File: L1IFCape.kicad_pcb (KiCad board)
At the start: 2 copper layers, 86.4 x 54.6 mm, 72 parts, among them J1 RF_Shield_One_Piece, J2 SMA, J3 MMCX, P8 BeagleBone_Black_Header, P9 BeagleBone_Black_Header, U1 24CS256, U2 MAX2769BETI+T, U3 MAX31343ETAY+T, U4 TPS717285DCK, U5 TPS717285DCK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

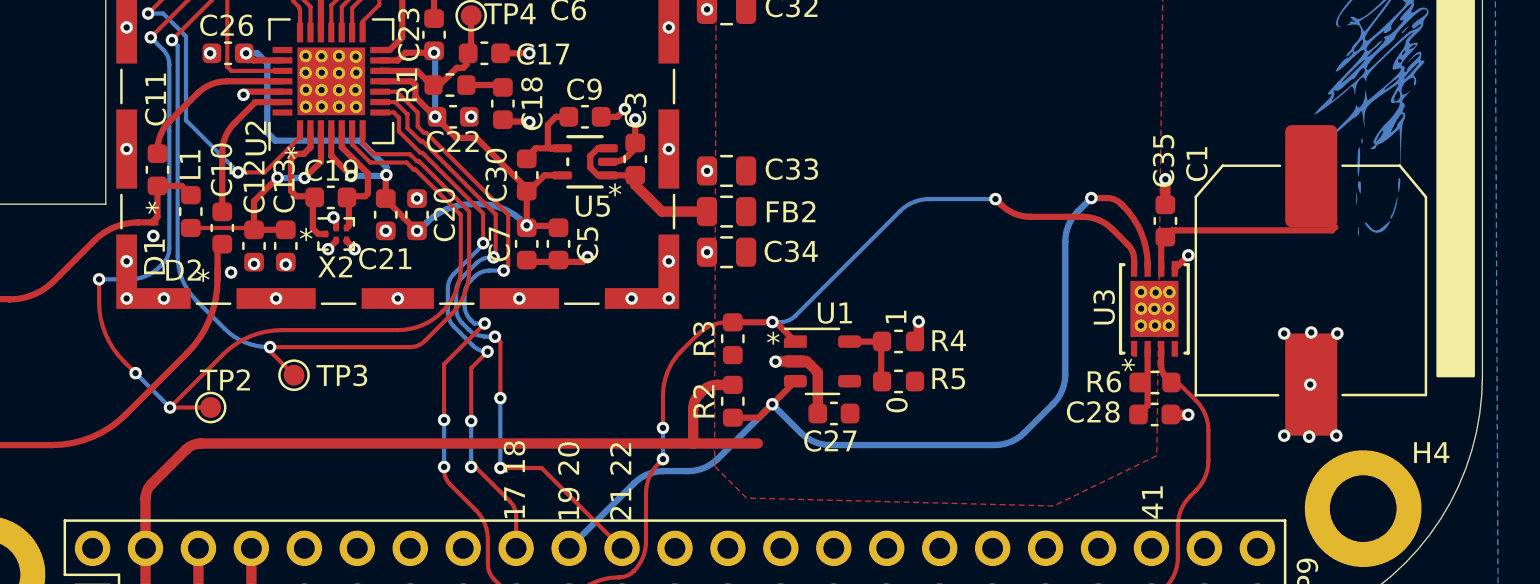
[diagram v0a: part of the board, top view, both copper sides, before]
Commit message: Added CERN License
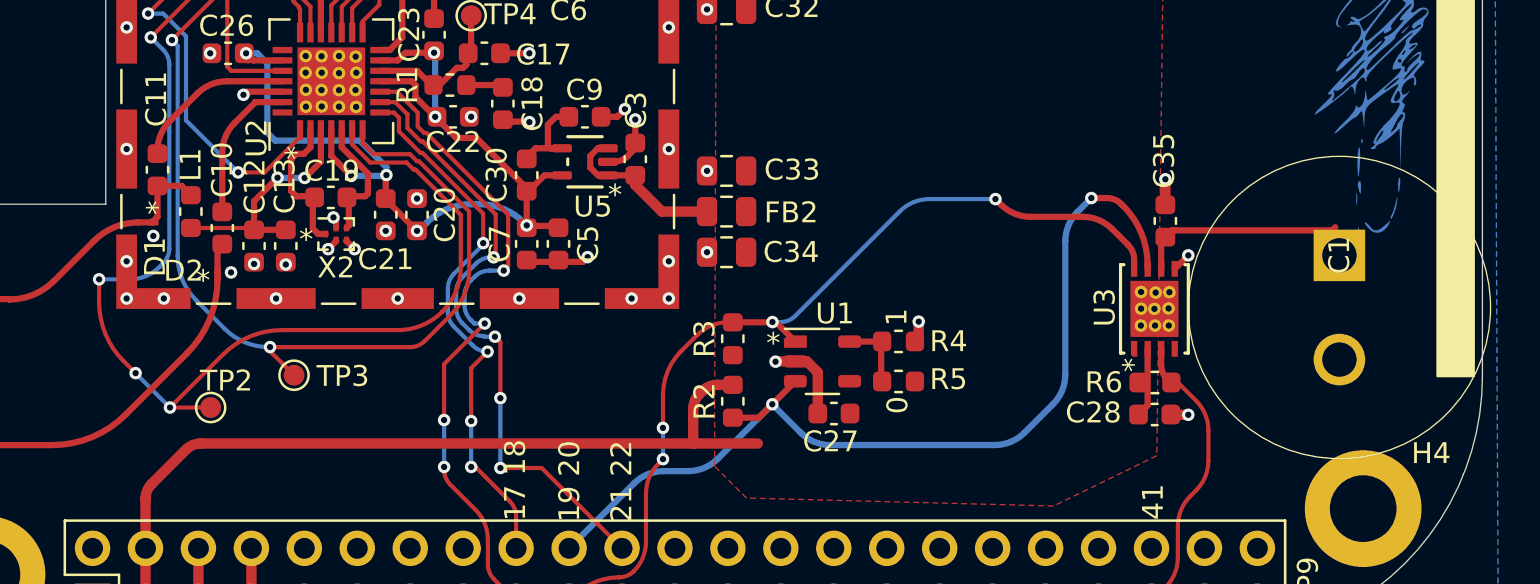
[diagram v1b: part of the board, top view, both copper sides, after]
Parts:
- C1: value 0.1 F -> 1F; footprint L1IF:C_EDLC_FCR_10.8x10.8 -> L1IF:CAPPRD500W145D1350H830
- moved C1 1.81 mm to (179.5, 81.5)
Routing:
- net GND: vias 69 -> 62

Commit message: Moved some parts around
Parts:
- moved TP2 34.4 mm to (125.8, 54.4)
- moved TP3 32.9 mm to (128.4, 54.4)
- moved C1 5.71 mm to (174.2, 83.8), turned to 0 degrees
- moved R6 3.48 mm to (167.9, 89.7)
- moved C35 3.07 mm to (168.1, 80.2)
- moved U3 3.07 mm to (167.6, 84.4)
- moved C28 2.93 mm to (167.9, 88.2)
- moved TP1 0.32 mm to (123.2, 54.4)
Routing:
- net /I2C0.SDA: track 46.5 -> 41.9 mm
- net /I2C0.SCL: track 42.7 -> 39.7 mm
- net /LD: track 77.1 -> 75.1 mm
- net /~{RTC_INTR}: track 14.8 -> 13.2 mm
- net /~{SHDN}: track 67.6 -> 66.0 mm
- net +3V3: track 43.1 -> 41.6 mm
- net Net-(U3-VBAT): track 9.95 -> 8.67 mm
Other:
- board text added: "*"

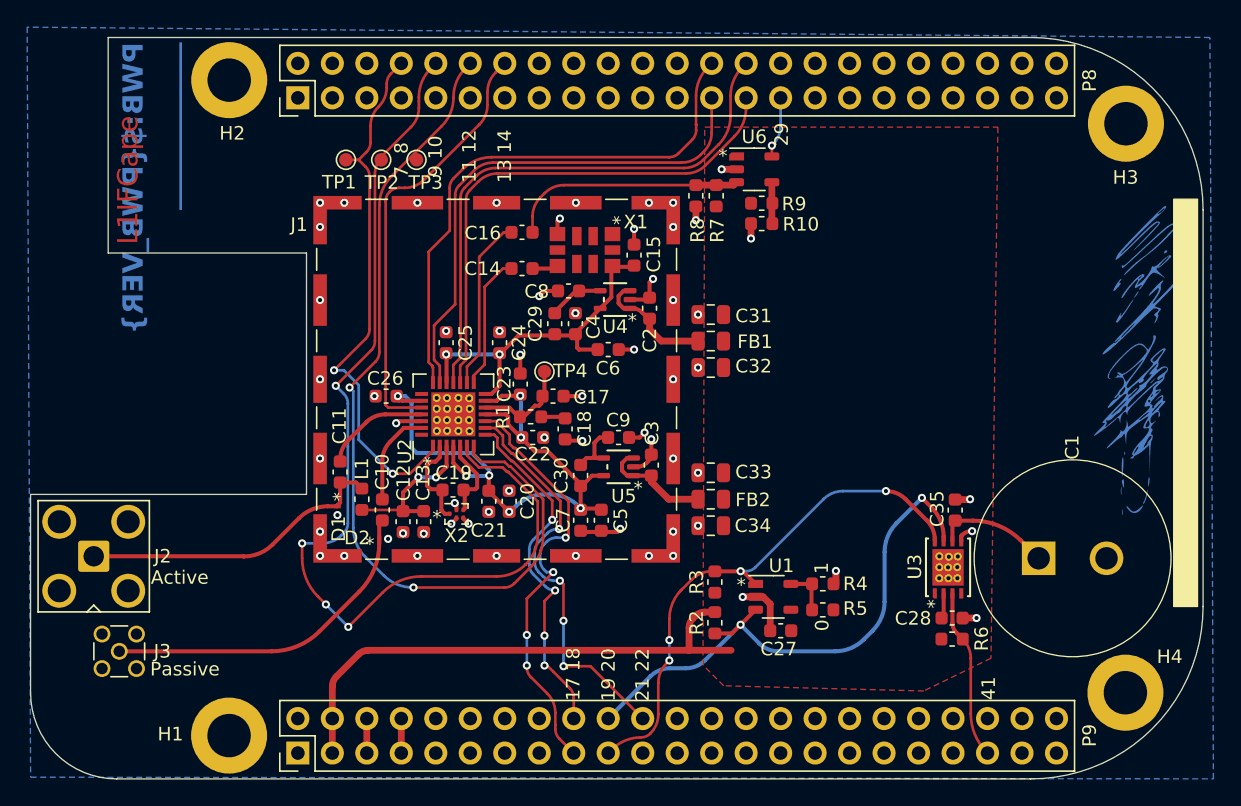
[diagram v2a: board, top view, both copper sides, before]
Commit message: Added Padlock graphic and 1F Supercap
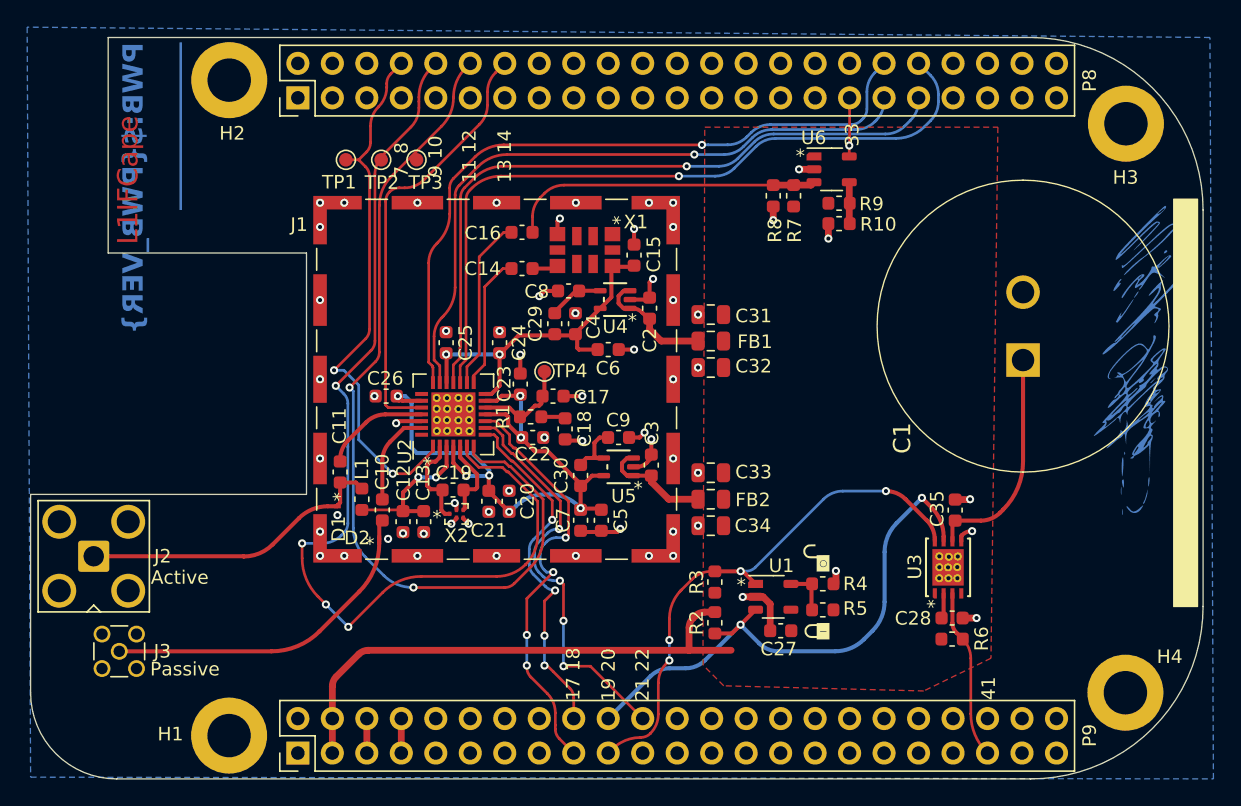
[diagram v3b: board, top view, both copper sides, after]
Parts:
- added G***: LOGO, L1IF:Padlock-On, F.Cu at (157.9, 88.7)
- added G***: LOGO, L1IF:Padlock-Off, F.Cu at (157.9, 83.7)
- C1: footprint L1IF:CAPPRD500W145D1350H830 -> L1IF:KR5R5C105R
- moved C1 14.6 mm to (173.1, 69.2), turned to 90 degrees
- moved R10 5.70 mm to (159.6, 59.1)
- moved R9 5.70 mm to (159.6, 57.6)
- moved R7 5.70 mm to (156.2, 57.0)
- moved R8 5.70 mm to (154.7, 57.0)
- moved U6 5.70 mm to (159.0, 55.1)
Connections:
- P8 pad 25: /SI0H -> unconnected-(P8-Pin_25-Pad25)
- P8 pad 26: /SI1H -> unconnected-(P8-Pin_26-Pad26)
- P8 pad 27: /SQ1H -> unconnected-(P8-Pin_27-Pad27)
- P8 pad 28: /SQ0H -> unconnected-(P8-Pin_28-Pad28)
- P8 pad 29: /BBClk -> unconnected-(P8-Pin_29-Pad29)
- P8 pad 33: /CLKIN_S_7 -> /BBClk
- P8 pad 35: /GPIO52PB1/LPRB_A -> /SI0H
- P8 pad 36: /GPIO37NB1 -> /SI1H
- P8 pad 37: /CCC_SW_CLKIN_S_1 -> /SQ0H
- P8 pad 38: /GPIO3NB1 -> /SQ1H
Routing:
- net /SQ1H: track 38.4 -> 54.9 mm, vias 0 -> 1
- net /SI1H: track 40.5 -> 51.8 mm, vias 0 -> 1
- net /SI0H: track 38.4 -> 49.2 mm, vias 0 -> 1
- net /SQ0H: track 41.0 -> 50.9 mm, vias 0 -> 1
- net Net-(U3-VBAT): track 8.67 -> 16.8 mm
- net /CLKO: track 17.8 -> 23.5 mm
- net unconnected-(P8-Pin_27-Pad27): track 0.00 -> 0.73 mm
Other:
- board text added: "33"
- board text removed: "0"
- board text removed: "1"
- board text removed: "29"

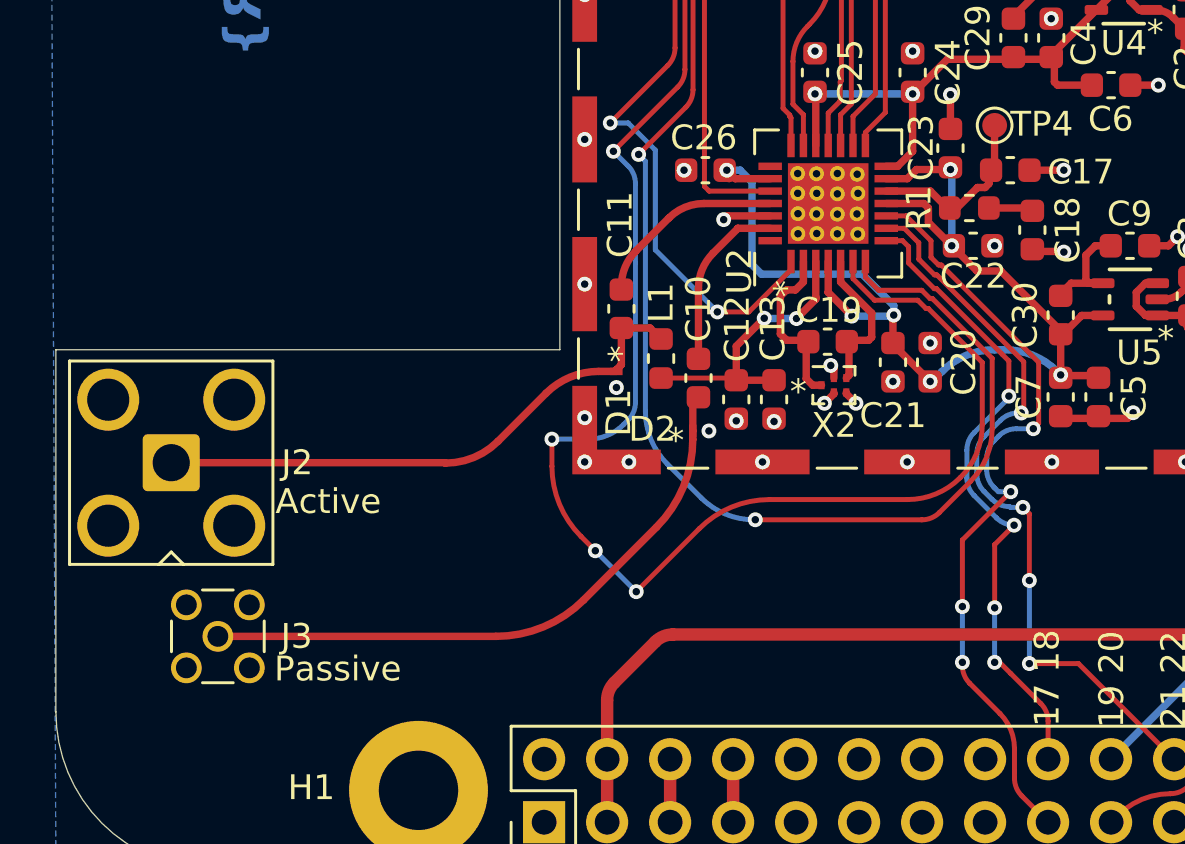
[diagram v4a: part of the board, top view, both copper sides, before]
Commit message: Moved Antenna Ports, and changed resistor bias circuit
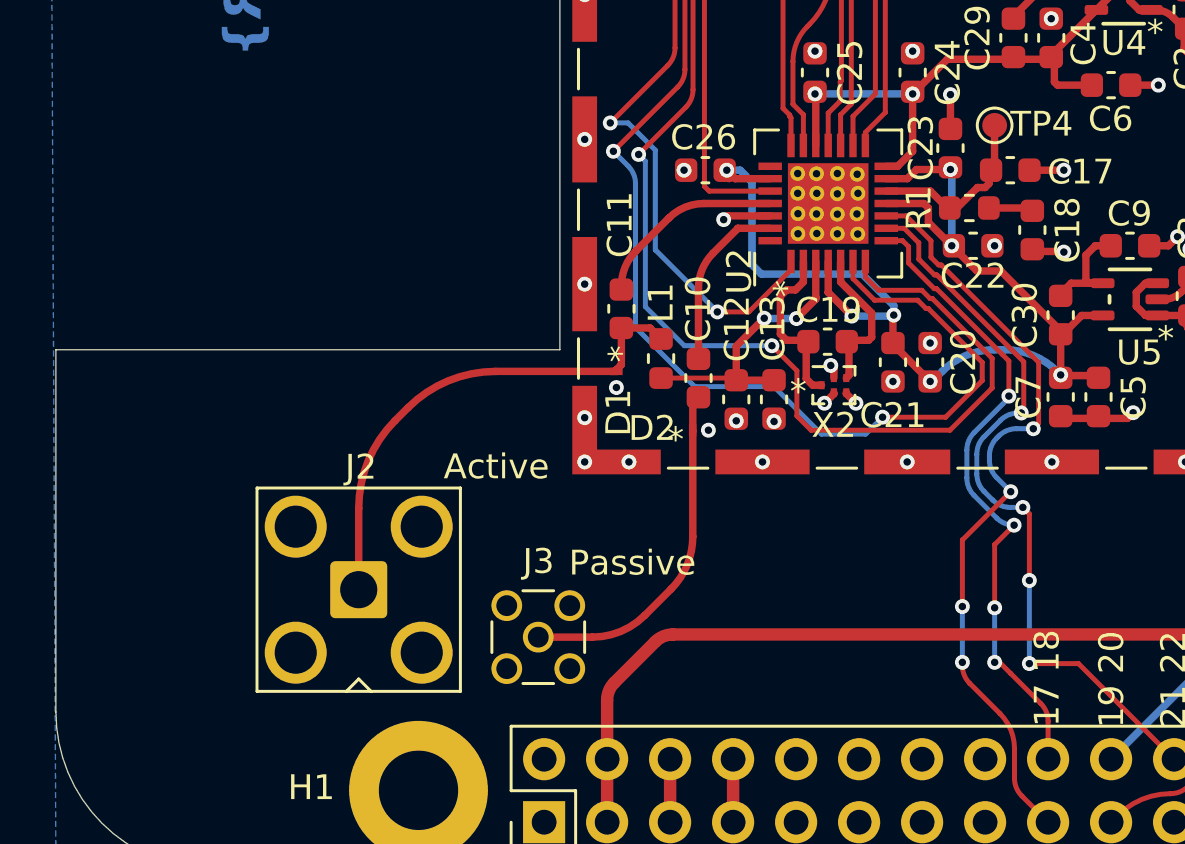
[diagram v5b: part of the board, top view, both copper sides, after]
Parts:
- moved J3 12.9 mm to (119.4, 90.6)
- moved J2 9.13 mm to (112.2, 88.7)
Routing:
- net /LD: track 75.1 -> 58.5 mm, vias 4 -> 2
- net Net-(D2-K): track 25.0 -> 14.1 mm
- net /~{SHDN}: track 66.0 -> 59.4 mm
- net Net-(D1-K): track 22.8 -> 20.3 mm
